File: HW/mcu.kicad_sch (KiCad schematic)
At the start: 10 parts, among them J2 JTAG, SW2 SW_DPST, SW3 SW_DPST, U1 ESP32-S2-MINI-2

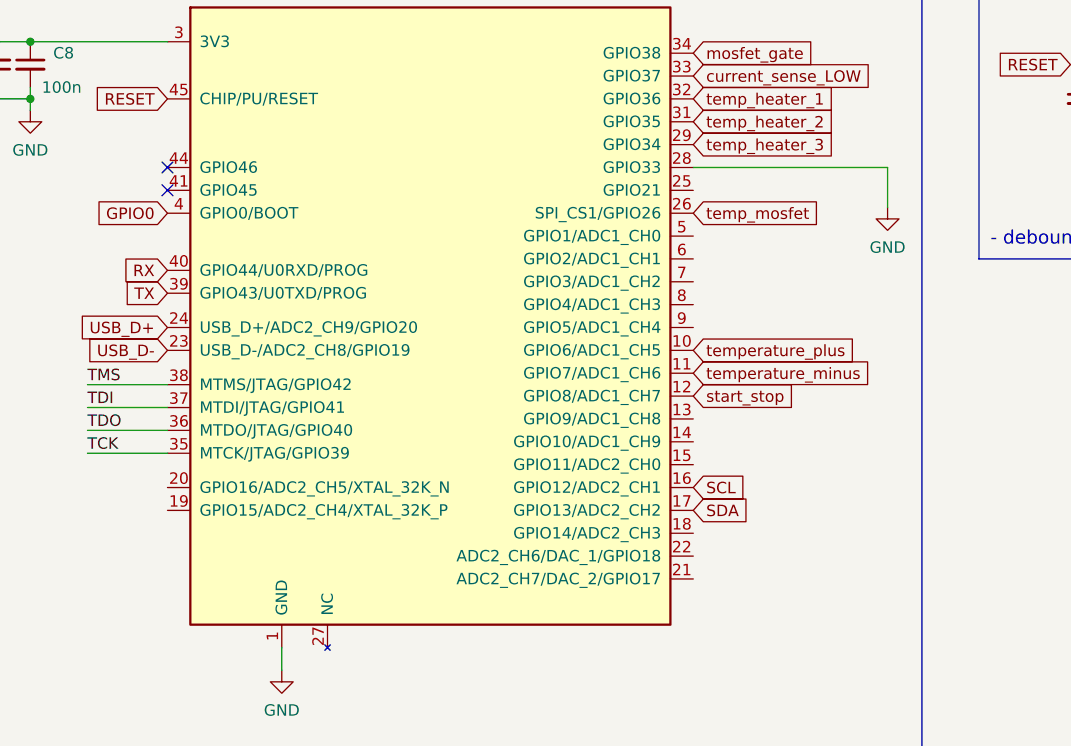
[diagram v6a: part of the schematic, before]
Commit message: Fix board, QOL fixes
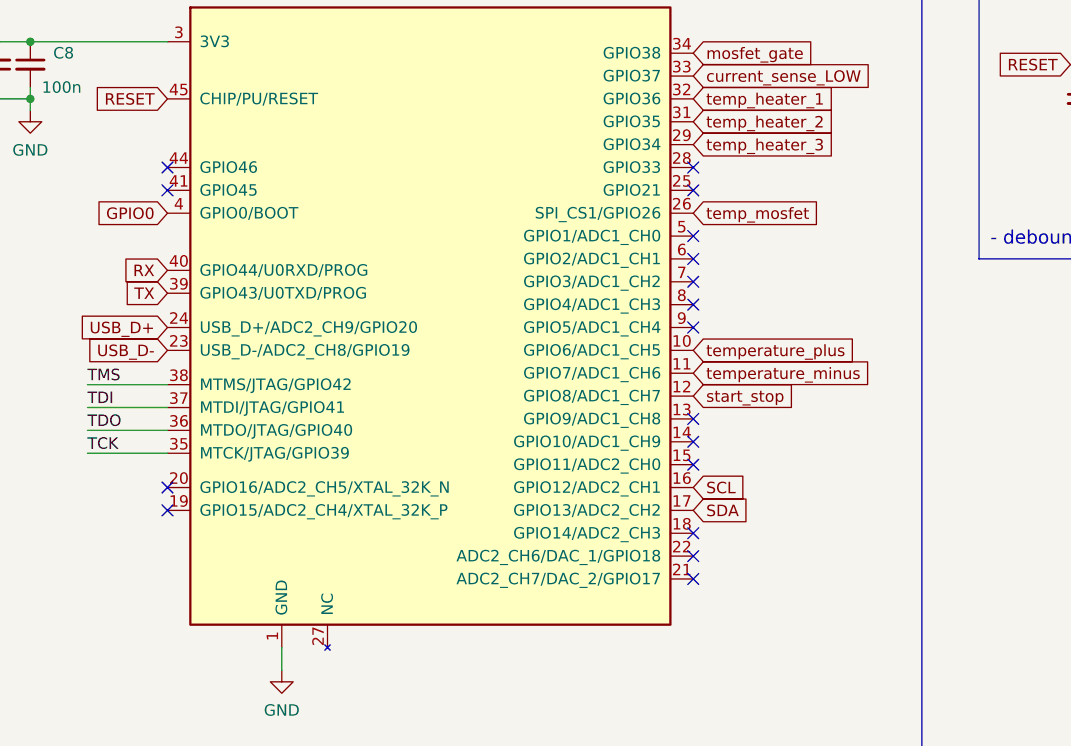
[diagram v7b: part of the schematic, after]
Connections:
- net GND: no longer U1.28 (GPIO33)
- no-connect marks 2 -> 17
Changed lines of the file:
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@@
   (junction (at 29.21 38.1) (diameter 0) (color 0 0 0 0)
   )
+  (no_connect (at 106.68 59.69))
+  (no_connect (at 106.68 82.55))
+  (no_connect (at 106.68 54.61))
+  (no_connect (at 106.68 69.85))
   (no_connect (at 48.26 54.61))
   (no_connect (at 48.26 52.07))
+  (no_connect (at 106.68 85.09))
+  (no_connect (at 106.68 64.77))
+  (no_connect (at 48.26 87.63))
+  (no_connect (at 106.68 52.07))
+  (no_connect (at 106.68 67.31))
+  (no_connect (at 106.68 97.79))
+  (no_connect (at 106.68 95.25))
+  (no_connect (at 48.26 90.17))
+  (no_connect (at 106.68 92.71))
+  (no_connect (at 106.68 80.01))
+  (no_connect (at 106.68 62.23))
   (wire (pts (xy 60.96 105.41) (xy 60.96 107.95))
     (stroke (width 0) (type default) (color 0 0 0 0))
@@
     (stroke (width 0) (type default) (color 0 0 0 0))
   )
-  (wire (pts (xy 106.68 52.07) (xy 128.27 52.07))
-    (stroke (width 0) (type default) (color 0 0 0 0))
-  )
   (wire (pts (xy 149.86 40.64) (xy 149.86 41.91))
     (stroke (width 0) (type default) (color 0 0 0 0))
@@
   )
   (wire (pts (xy 163.83 35.56) (xy 161.29 35.56))
-    (stroke (width 0) (type default) (color 0 0 0 0))
-  )
-  (wire (pts (xy 128.27 52.07) (xy 128.27 56.515))
     (stroke (width 0) (type default) (color 0 0 0 0))
   )
@@
       (effects (font (size 1.27 1.27)) hide)
     )
-    (pin "1")
-  )
-  (symbol (lib_id "power:GND") (at 128.27 56.515 0) (unit 1)
-    (in_bom yes) (on_board yes) (fields_autoplaced)
-    (property "Reference" "#PWR0129" (id 0) (at 128.27 62.865 0)
-      (effects (font (size 1.27 1.27)) hide)
-    )
-    (property "Value" "GND" (id 1) (at 128.27 60.9584 0))
-    (property "Footprint" "" (id 2) (at 128.27 56.515 0)
-      (effects (font (size 1.27 1.27)) hide)
-    )
-    (property "Datasheet" "" (id 3) (at 128.27 56.515 0)
-      (effects (font (size 1.27 1.27)) hide)
-    )

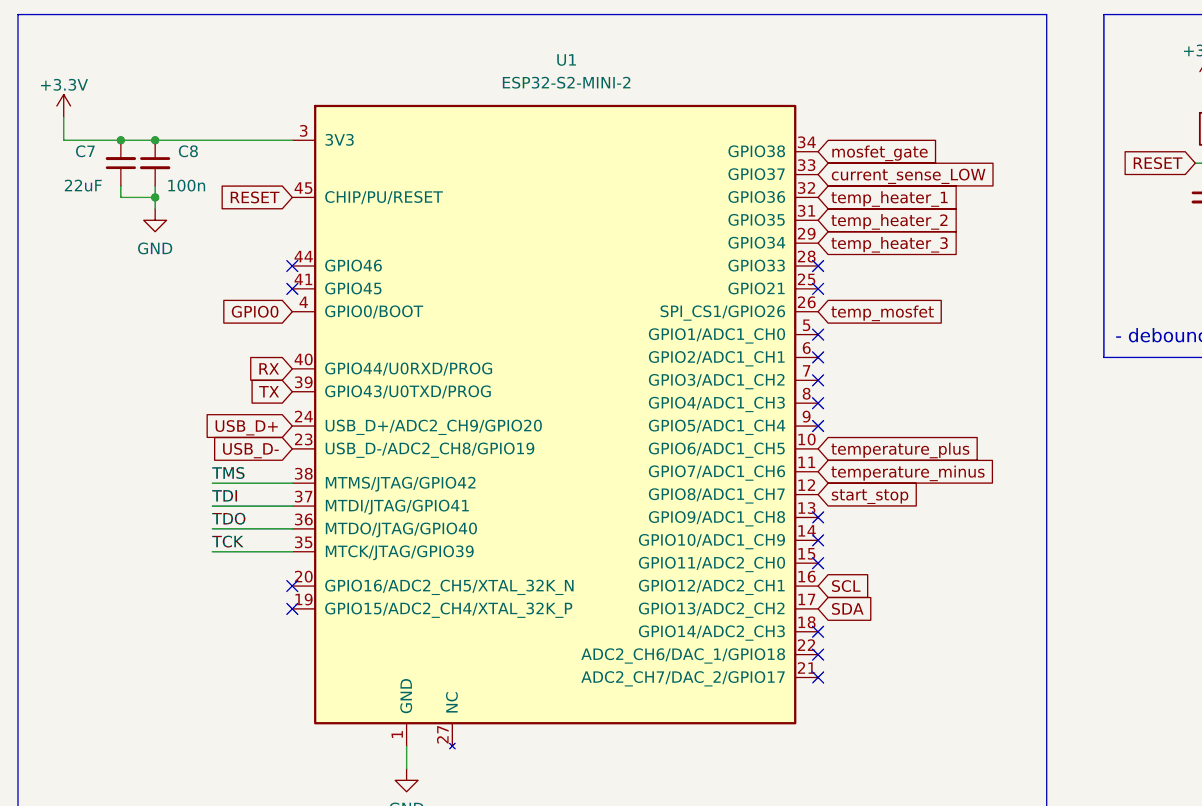
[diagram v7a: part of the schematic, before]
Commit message: QOL changes on pcb, fixed wrong ACDC brick polarity xD
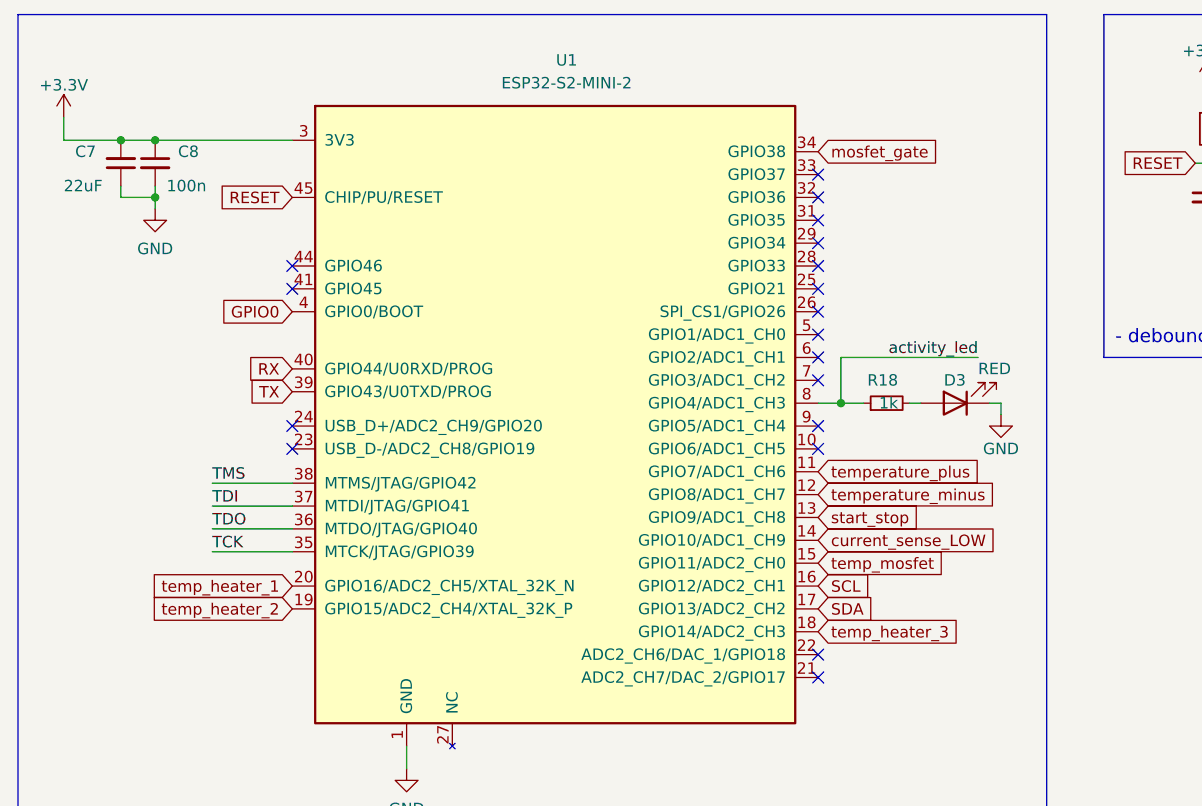
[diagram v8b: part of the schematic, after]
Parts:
- added D3: RED, LED_SMD:LED_0603_1608Metric, symbol Device:LED
- added R18: 1k, Resistor_SMD:R_0603_1608Metric, symbol Device:R_Small
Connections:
- net GND: now also D3.1 (K)
- net current_sense_LOW: now also U1.14 (GPIO10/ADC1_CH9); no longer U1.33 (GPIO37)
- net start_stop: now also U1.13 (GPIO9/ADC1_CH8); no longer U1.12 (GPIO8/ADC1_CH7)
- net temp_heater_1: now also U1.20 (GPIO16/ADC2_CH5/XTAL_32K_N); no longer U1.32 (GPIO36)
- net temp_heater_2: now also U1.19 (GPIO15/ADC2_CH4/XTAL_32K_P); no longer U1.31 (GPIO35)
- net temp_heater_3: now also U1.18 (GPIO14/ADC2_CH3); no longer U1.29 (GPIO34)
- net temp_mosfet: now also U1.15 (GPIO11/ADC2_CH0); no longer U1.26 (SPI_CS1/GPIO26)
- net temperature_minus: now also U1.12 (GPIO8/ADC1_CH7); no longer U1.11 (GPIO7/ADC1_CH6)
- net temperature_plus: now also U1.11 (GPIO7/ADC1_CH6); no longer U1.10 (GPIO6/ADC1_CH5)
- net activity_led: now reaches U1.8 (GPIO4/ADC1_CH3)
- net activity_led: now also R18.1
- net USB_D+: no longer names the net of U1.24 (USB_D+/ADC2_CH9/GPIO20)
- net USB_D-: no longer names the net of U1.23 (USB_D-/ADC2_CH8/GPIO19)
- new net: D3.2 (A), R18.2
- no-connect marks 17 -> 18
